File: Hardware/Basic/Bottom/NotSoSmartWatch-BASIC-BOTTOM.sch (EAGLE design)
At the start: 31 parts, among them U1 AD5242-SO16

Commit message: updated partially through Take 003
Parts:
- added J1: (no value), LinnesLab-Connectors:CONN_07
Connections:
- removed net LED.CTRL: U$4.A
- removed net PPG: C21.2, OP3G$1.OUT, U1.B2
- removed net TIA: C10.2, C15.1, OP4G$1.OUT, U1.W1
- new net A6/TIA: C10.2, C15.1, J1.5, OP4G$1.OUT, U1.W1
- new net A7/PPG: C21.2, J1.7, OP3G$1.OUT, U1.B2
- new net D29/LED.CTRL: J1.6, U$4.A
- net 3.3V: now also J1.2
- net GND: now also J1.1
- net SCL: now also J1.3
- net SDA: now also J1.4
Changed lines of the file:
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@@
 <part name="GND2" library="LinnesLab-Symbols" deviceset="GND" device=""/>
 <part name="SUPPLY3" library="LinnesLab-Symbols" deviceset="3.3V" device=""/>
+<part name="J1" library="LinnesLab-Connectors" deviceset="CONN_07" device=""/>
+<part name="GND3" library="LinnesLab-Symbols" deviceset="GND" device=""/>
+<part name="SUPPLY1" library="LinnesLab-Symbols" deviceset="3.3V" device=""/>
 </parts>
 <sheets>
@@
 <attribute name="VALUE" x="27.94" y="25.654" size="1.778" layer="96" align="bottom-center"/>
 </instance>
+<instance part="J1" gate="G$1" x="142.24" y="2.54" smashed="yes">
+<attribute name="VALUE" x="137.16" y="-7.366" size="1.778" layer="96" font="vector"/>
+<attribute name="NAME" x="137.16" y="15.748" size="1.778" layer="95" font="vector"/>
+</instance>
+<instance part="GND3" gate="G$1" x="154.94" y="-7.62" smashed="yes">
+<attribute name="VALUE" x="154.94" y="-7.874" size="1.778" layer="96" align="top-center"/>
+</instance>
+<instance part="SUPPLY1" gate="G$1" x="157.48" y="0" smashed="yes" rot="R270">
+<attribute name="VALUE" x="160.274" y="0" size="1.778" layer="96" rot="R270" align="bottom-center"/>
+</instance>
 </instances>
 <busses>
@@
 <wire x1="27.94" y1="10.16" x2="27.94" y2="12.7" width="0.1524" layer="91"/>
 </segment>
+<segment>
+<pinref part="J1" gate="G$1" pin="1"/>
+<wire x1="147.32" y1="-2.54" x2="154.94" y2="-2.54" width="0.1524" layer="91"/>
+<pinref part="GND3" gate="G$1" pin="GND"/>
+<wire x1="154.94" y1="-2.54" x2="154.94" y2="-5.08" width="0.1524" layer="91"/>
+</segment>
 </net>
 <net name="3.3V" class="0">
@@
 <wire x1="27.94" y1="22.86" x2="27.94" y2="20.32" width="0.1524" layer="91"/>
 </segment>
+<segment>
+<pinref part="J1" gate="G$1" pin="2"/>
+<pinref part="SUPPLY1" gate="G$1" pin="3.3V"/>
+<wire x1="157.48" y1="0" x2="147.32" y2="0" width="0.1524" layer="91"/>
+</segment>
 </net>
 <net name="SDA" class="0">
@@
 <label x="68.58" y="17.78" size="1.27" layer="95" xref="yes"/>
 </segment>
+<segment>
+<pinref part="J1" gate="G$1" pin="4"/>
+<wire x1="147.32" y1="5.08" x2="149.86" y2="5.08" width="0.1524" layer="91"/>
+<label x="149.86" y="5.08" size="1.016" layer="95" xref="yes"/>
+</segment>
 </net>
 <net name="SCL" class="0">
@@
 <label x="68.58" y="12.7" size="1.27" layer="95" xref="yes"/>
 </segment>
-</net>
-<net name="TIA" class="0">
+<segment>
+<pinref part="J1" gate="G$1" pin="3"/>
+<wire x1="147.32" y1="2.54" x2="149.86" y2="2.54" width="0.1524" layer="91"/>
+<label x="149.86" y="2.54" size="1.016" layer="95" xref="yes"/>
+</segment>
+</net>
+<net name="A6/TIA" class="0">
 <segment>
 <wire x1="142.24" y1="58.42" x2="137.16" y2="58.42" width="0.1524" layer="91"/>
@@
 <junction x="88.9" y="124.46"/>
 </segment>
+<segment>
+<pinref part="J1" gate="G$1" pin="5"/>
+<wire x1="147.32" y1="7.62" x2="149.86" y2="7.62" width="0.1524" layer="91"/>
+<label x="149.86" y="7.62" size="1.016" layer="95" xref="yes"/>
+</segment>
 </net>
 <net name="PD.C" class="0">
@@
 </segment>
 </net>
-<net name="LED.CTRL" class="0">
+<net name="D29/LED.CTRL" class="0">
 <segment>
 <pinref part="U$4" gate="G$1" pin="A"/>
@@
 <wire x1="238.76" y1="60.96" x2="238.76" y2="68.58" width="0.1524" layer="91"/>
 <label x="238.76" y="68.58" size="1.27" layer="95" rot="R180" xref="yes"/>
+</segment>
+<segment>
+<pinref part="J1" gate="G$1" pin="6"/>
+<wire x1="147.32" y1="10.16" x2="149.86" y2="10.16" width="0.1524" layer="91"/>
+<label x="149.86" y="10.16" size="1.016" layer="95" xref="yes"/>
 </segment>
 </net>
@@
 </segment>
 </net>
-<net name="PPG" class="0">
+<net name="A7/PPG" class="0">
 <segment>
 <wire x1="170.18" y1="58.42" x2="172.72" y2="58.42" width="0.1524" layer="91"/>
@@
 <label x="228.6" y="116.84" size="1.27" layer="95" xref="yes"/>
 </segment>
-</net>
+<segment>
+<pinref part="J1" gate="G$1" pin="7"/>
+<wire x1="147.32" y1="12.7" x2="149.86" y2="12.7" width="0.1524" layer="91"/>
+<label x="149.86" y="12.7" size="1.016" layer="95" xref="yes"/>
+</segment>
+</net>

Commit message: still working through Take 003
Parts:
- J1: device LinnesLab-Connectors:CONN_07 -> LinnesLab-Connectors:CONN_07-1.27MM
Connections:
- net 3.3V: now also J1.4; no longer J1.2
- net GND: now also J1.3; no longer J1.1
- net SCL: now also J1.2; no longer J1.3
- net SDA: now also J1.1; no longer J1.4
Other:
- note added: "Header Pins"
- moved on the sheet: J1
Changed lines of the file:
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@@
 <part name="GND2" library="LinnesLab-Symbols" deviceset="GND" device=""/>
 <part name="SUPPLY3" library="LinnesLab-Symbols" deviceset="3.3V" device=""/>
-<part name="J1" library="LinnesLab-Connectors" deviceset="CONN_07" device=""/>
+<part name="J1" library="LinnesLab-Connectors" deviceset="CONN_07" device="-1.27MM"/>
+<part name="SUPPLY1" library="LinnesLab-Symbols" deviceset="3.3V" device=""/>
 <part name="GND3" library="LinnesLab-Symbols" deviceset="GND" device=""/>
-<part name="SUPPLY1" library="LinnesLab-Symbols" deviceset="3.3V" device=""/>
 </parts>
 <sheets>
@@
 <text x="144.78" y="35.56" size="1.778" layer="97" ratio="15">I2C Address: 0x2C</text>
 <text x="210.82" y="38.1" size="1.778" layer="97" ratio="15">I2C Address: 0x2D</text>
+<text x="137.16" y="10.16" size="2.54" layer="97" font="vector" ratio="15">Header Pins</text>
 </plain>
 <instances>
@@
 <attribute name="VALUE" x="27.94" y="25.654" size="1.778" layer="96" align="bottom-center"/>
 </instance>
-<instance part="J1" gate="G$1" x="142.24" y="2.54" smashed="yes">
-<attribute name="VALUE" x="137.16" y="-7.366" size="1.778" layer="96" font="vector"/>
-<attribute name="NAME" x="137.16" y="15.748" size="1.778" layer="95" font="vector"/>
-</instance>
-<instance part="GND3" gate="G$1" x="154.94" y="-7.62" smashed="yes">
-<attribute name="VALUE" x="154.94" y="-7.874" size="1.778" layer="96" align="top-center"/>
-</instance>
-<instance part="SUPPLY1" gate="G$1" x="157.48" y="0" smashed="yes" rot="R270">
-<attribute name="VALUE" x="160.274" y="0" size="1.778" layer="96" rot="R270" align="bottom-center"/>
+<instance part="J1" gate="G$1" x="142.24" y="-17.78" smashed="yes">
+<attribute name="VALUE" x="137.16" y="-27.686" size="1.778" layer="96" font="vector"/>
+<attribute name="NAME" x="137.16" y="-4.572" size="1.778" layer="95" font="vector"/>
+</instance>
+<instance part="SUPPLY1" gate="G$1" x="152.4" y="-2.54" smashed="yes">
+<attribute name="VALUE" x="152.4" y="0.254" size="1.778" layer="96" align="bottom-center"/>
+</instance>
+<instance part="GND3" gate="G$1" x="152.4" y="-30.48" smashed="yes">
+<attribute name="VALUE" x="152.4" y="-30.734" size="1.778" layer="96" align="top-center"/>
 </instance>
 </instances>
@@
 </segment>
 <segment>
-<pinref part="J1" gate="G$1" pin="1"/>
-<wire x1="147.32" y1="-2.54" x2="154.94" y2="-2.54" width="0.1524" layer="91"/>
+<pinref part="J1" gate="G$1" pin="3"/>
+<wire x1="147.32" y1="-17.78" x2="152.4" y2="-17.78" width="0.1524" layer="91"/>
 <pinref part="GND3" gate="G$1" pin="GND"/>
-<wire x1="154.94" y1="-2.54" x2="154.94" y2="-5.08" width="0.1524" layer="91"/>
+<wire x1="152.4" y1="-17.78" x2="152.4" y2="-27.94" width="0.1524" layer="91"/>
 </segment>
 </net>
@@
 </segment>
 <segment>
-<pinref part="J1" gate="G$1" pin="2"/>
+<pinref part="J1" gate="G$1" pin="4"/>
+<wire x1="147.32" y1="-15.24" x2="152.4" y2="-15.24" width="0.1524" layer="91"/>
 <pinref part="SUPPLY1" gate="G$1" pin="3.3V"/>
-<wire x1="157.48" y1="0" x2="147.32" y2="0" width="0.1524" layer="91"/>
+<wire x1="152.4" y1="-15.24" x2="152.4" y2="-2.54" width="0.1524" layer="91"/>
 </segment>
 </net>
@@
 </segment>
 <segment>
-<pinref part="J1" gate="G$1" pin="4"/>
-<wire x1="147.32" y1="5.08" x2="149.86" y2="5.08" width="0.1524" layer="91"/>
-<label x="149.86" y="5.08" size="1.016" layer="95" xref="yes"/>
+<pinref part="J1" gate="G$1" pin="1"/>
+<wire x1="147.32" y1="-22.86" x2="157.48" y2="-22.86" width="0.1524" layer="91"/>
+<label x="157.48" y="-22.86" size="1.27" layer="95" xref="yes"/>
 </segment>
 </net>
@@
 </segment>
 <segment>
-<pinref part="J1" gate="G$1" pin="3"/>
-<wire x1="147.32" y1="2.54" x2="149.86" y2="2.54" width="0.1524" layer="91"/>
-<label x="149.86" y="2.54" size="1.016" layer="95" xref="yes"/>
+<pinref part="J1" gate="G$1" pin="2"/>
+<wire x1="147.32" y1="-20.32" x2="157.48" y2="-20.32" width="0.1524" layer="91"/>
+<label x="157.48" y="-20.32" size="1.27" layer="95" xref="yes"/>
 </segment>
 </net>
@@
 <segment>
 <pinref part="J1" gate="G$1" pin="5"/>
-<wire x1="147.32" y1="7.62" x2="149.86" y2="7.62" width="0.1524" layer="91"/>
-<label x="149.86" y="7.62" size="1.016" layer="95" xref="yes"/>
+<wire x1="147.32" y1="-12.7" x2="157.48" y2="-12.7" width="0.1524" layer="91"/>
+<label x="157.48" y="-12.7" size="1.27" layer="95" xref="yes"/>
 </segment>
 </net>
@@
 <segment>
 <pinref part="J1" gate="G$1" pin="6"/>
-<wire x1="147.32" y1="10.16" x2="149.86" y2="10.16" width="0.1524" layer="91"/>
-<label x="149.86" y="10.16" size="1.016" layer="95" xref="yes"/>
+<wire x1="147.32" y1="-10.16" x2="157.48" y2="-10.16" width="0.1524" layer="91"/>
+<label x="157.48" y="-10.16" size="1.27" layer="95" xref="yes"/>
 </segment>
 </net>
@@
 <segment>
 <pinref part="J1" gate="G$1" pin="7"/>
-<wire x1="147.32" y1="12.7" x2="149.86" y2="12.7" width="0.1524" layer="91"/>
-<label x="149.86" y="12.7" size="1.016" layer="95" xref="yes"/>
-</segment>
-</net>
+<wire x1="147.32" y1="-7.62" x2="157.48" y2="-7.62" width="0.1524" layer="91"/>
+<label x="157.48" y="-7.62" size="1.27" layer="95" xref="yes"/>
+</segment>
+</net>

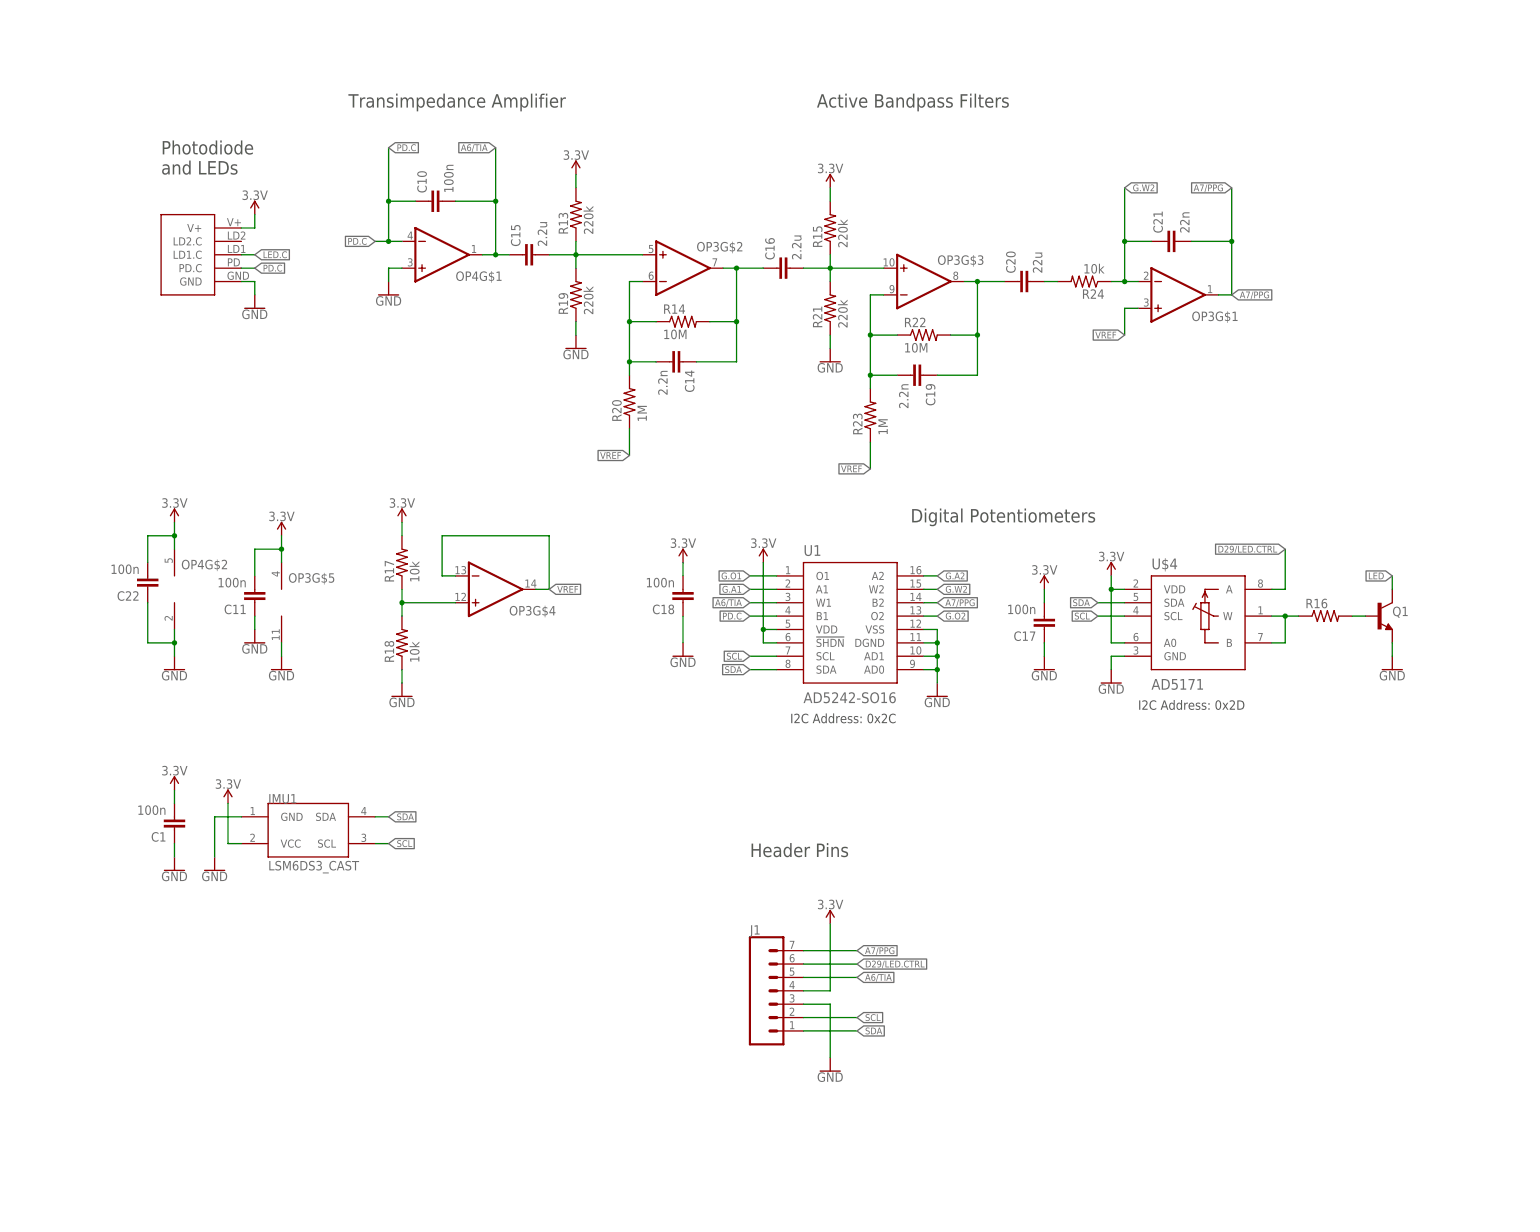
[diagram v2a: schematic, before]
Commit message: updated through Take 003 - worried I might have isolated polygon
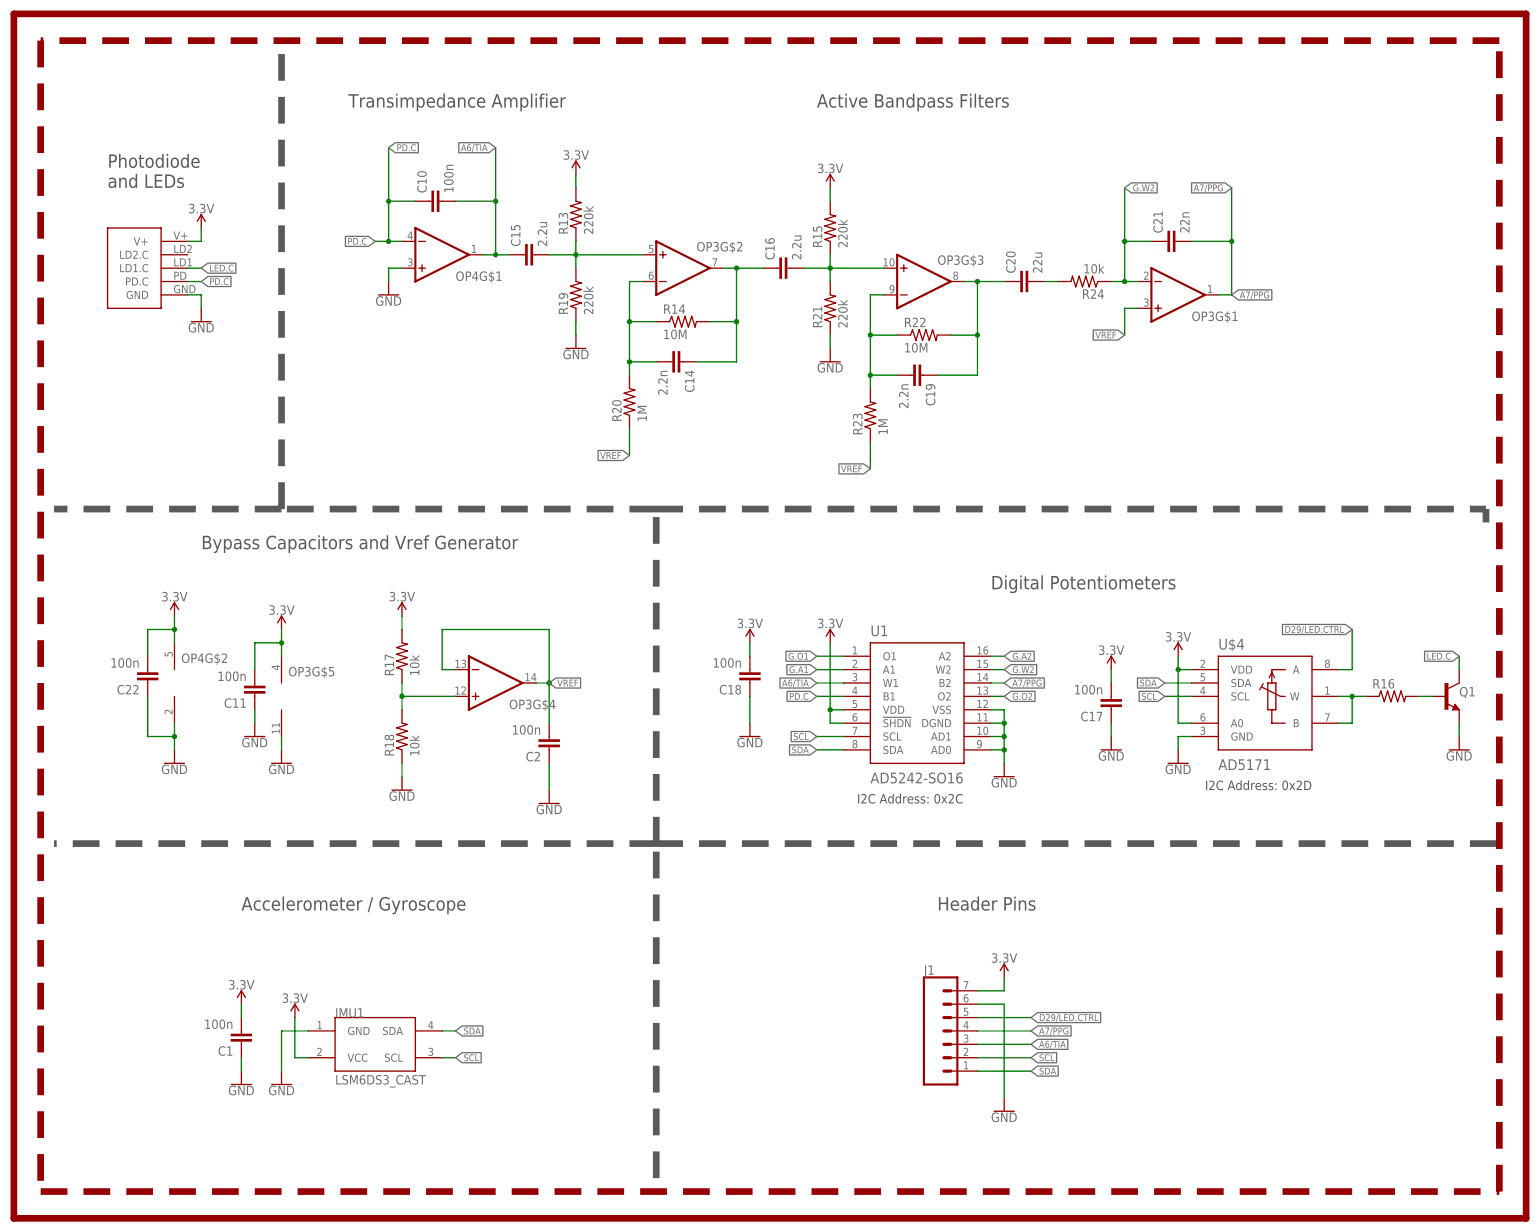
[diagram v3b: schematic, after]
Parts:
- added C2: 100n, LinnesLab-Passives:CAPACITOR0603
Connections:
- removed net LED: Q1.C
- net 3.3V: now also J1.7; no longer J1.4
- net A6/TIA: now also J1.3; no longer J1.5
- net A7/PPG: now also J1.4; no longer J1.7
- net D29/LED.CTRL: now also J1.5; no longer J1.6
- net GND: now also C2.1, J1.6; no longer J1.3
- net LED.C: now also Q1.C
- net VREF: now also C2.2
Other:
- note added: "Accelerometer / Gyroscope"
- note added: "Bypass Capacitors and Vref Generator"
- moved on the sheet: C1, C11, C17, C18, C22, IMU1, J1, OP3G$4, OP3G$5, OP4G$2, Q1, R16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
